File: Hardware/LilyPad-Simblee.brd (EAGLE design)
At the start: 45.3 x 45.2 mm, 37 parts, among them U1 MIC5219 3.3V, U2 MCP73831, U3 RFD77101

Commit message: Rep D8 w D6, add pour to antenna area, pour to top
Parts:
- moved C1 2.41 mm to (-17.3, -5.08)
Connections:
- removed net D8: A4/18.1, U3.20
- new net D6: A4/18.1, U3.31
- new net ISO_PAD: U3.1, U3.2, U3.4
- net GND: no longer U3.1, U3.2, U3.4
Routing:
- net D8: track 64.1 -> 0.00 mm, vias 1 -> 0
- net D6: track 0.00 -> 31.5 mm, vias 0 -> 1
- net ISO_PAD: track 0.00 -> 3.52 mm
- net GND: track 42.6 -> 41.0 mm, vias 15 -> 14
- net RST: track 52.7 -> 53.9 mm, vias 4 -> 5
- net 3.3V: track 39.8 -> 39.0 mm
- added copper zone on layer 1, net GND
- added copper zone on layer 1, net ISO_PAD

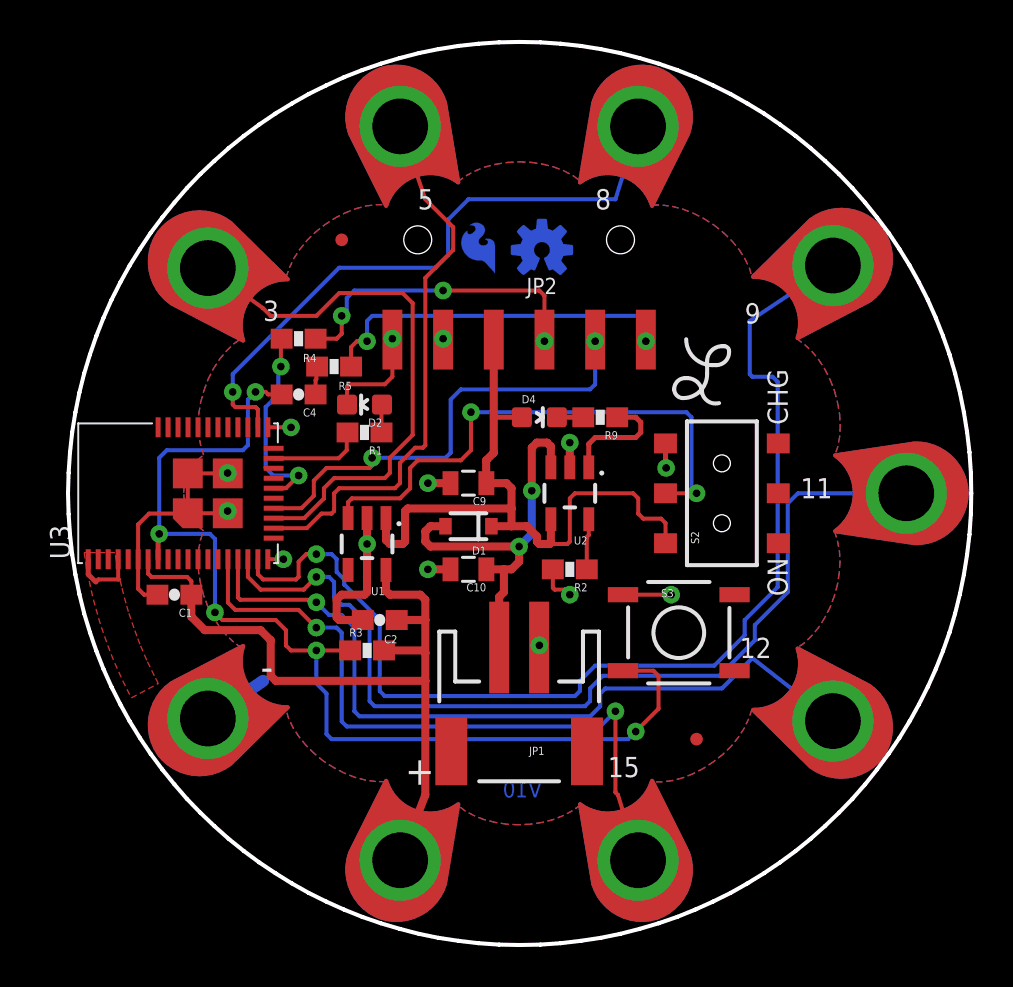
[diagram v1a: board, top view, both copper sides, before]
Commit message: Fix some QC review issues
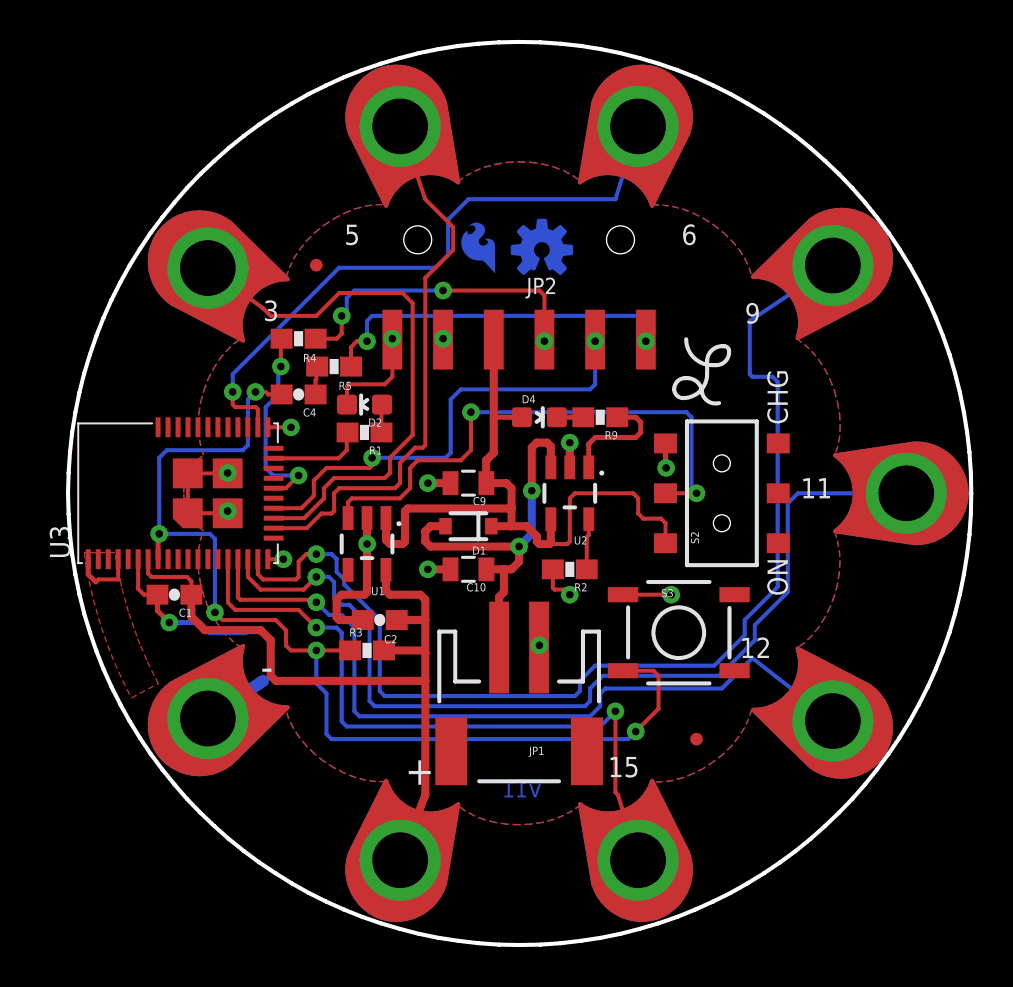
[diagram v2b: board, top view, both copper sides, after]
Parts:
- moved FID1 1.80 mm to (-10.2, 11.4)
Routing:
- net GND: track 41.0 -> 42.4 mm, vias 14 -> 15
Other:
- board text added: "6"
- board text added: "V11"
- board text removed: "8"
- board text removed: "V10"
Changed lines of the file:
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@@
 <wire x1="22.6364" y1="1.026125" x2="22.6564" y2="-0.003875" width="0.2032" layer="20"/>
 <text x="-12.827" y="8.636" size="1.016" layer="21" font="vector" ratio="15">3</text>
-<text x="-5.08" y="14.224" size="1.016" layer="21" font="vector" ratio="15">5</text>
-<text x="3.81" y="14.224" size="1.016" layer="21" font="vector" ratio="15">8</text>
+<text x="-8.763" y="12.446" size="1.016" layer="21" font="vector" ratio="15">5</text>
+<text x="8.128" y="12.446" size="1.016" layer="21" font="vector" ratio="15">6</text>
 <text x="11.303" y="8.509" size="1.016" layer="21" font="vector" ratio="15">9</text>
 <text x="14.097" y="-0.254" size="1.016" layer="21" font="vector" ratio="15">11</text>
@@
 <text x="-5.715" y="-14.605" size="1.4224" layer="21" font="vector" ratio="15">+</text>
 <text x="-12.954" y="-9.398" size="1.4224" layer="21" font="vector" ratio="15">-</text>
-<text x="1.143" y="-15.24" size="0.8128" layer="16" font="vector" ratio="15" rot="MR0">V10</text>
+<text x="1.143" y="-15.24" size="0.8128" layer="16" font="vector" ratio="15" rot="MR0">V11</text>
 <text x="22.86" y="-24.13" size="1.778" layer="51" font="vector" ratio="15">NOTE: Use 0.032" board thickness!</text>
 <text x="73.66" y="-31.75" size="1.778" layer="51" font="vector" ratio="15">Mike Hord</text>
@@
 <element name="LOGO1" library="SparkFun-Aesthetics" package="SFE_LOGO_FLAME_COPPER_.1" value="SFE_LOGO_FLAME.1COP" x="-0.889" y="10.668" rot="MR0"/>
 <element name="LOGO2" library="SparkFun-Aesthetics" package="OSHW-LOGO-S_COPPER" value="OSHW-LOGOS-COPPER" x="1.143" y="12.192" rot="MR0"/>
-<element name="FID1" library="SparkFun-Aesthetics" package="MICRO-FIDUCIAL" value="FIDUCIALUFIDUCIAL" x="-8.89" y="12.7"/>
+<element name="FID1" library="SparkFun-Aesthetics" package="MICRO-FIDUCIAL" value="FIDUCIALUFIDUCIAL" x="-10.16" y="11.43"/>
 <element name="FID2" library="SparkFun-Aesthetics" package="MICRO-FIDUCIAL" value="FIDUCIALUFIDUCIAL" x="8.89" y="-12.319"/>
 <element name="U$1" library="LilyPad-Wearables" package="LOGO-L" value="LOGO-LPL" x="9.144" y="6.096"/>
@@
 <wire x1="-18.796" y1="-5.08" x2="-19.09" y2="-4.786" width="0.2032" layer="1"/>
 <wire x1="-19.09" y1="-3.302" x2="-19.09" y2="-4.786" width="0.2032" layer="1"/>
-<wire x1="-19.09" y1="-3.302" x2="-19.09" y2="-1.564" width="0.2032" layer="1"/>
-<wire x1="-19.09" y1="-1.564" x2="-18.542" y2="-1.016" width="0.2032" layer="1"/>
-<wire x1="-18.542" y1="-1.016" x2="-16.614" y2="-1.016" width="0.2032" layer="1"/>
-<wire x1="-16.614" y1="-1.016" x2="-16.6" y2="-1.002" width="0.2032" layer="1"/>
 <polygon width="0.203" layer="1" isolate="0.3048" orphans="yes">
 <vertex x="-14.31" y="-7.45"/>
@@
 <vertex x="-13.92" y="-7.74"/>
 </polygon>
+<wire x1="-18.122" y1="-5.08" x2="-18.122" y2="-5.881" width="0.254" layer="1"/>
+<wire x1="-18.122" y1="-5.881" x2="-17.526" y2="-6.477" width="0.254" layer="1"/>
+<via x="-17.526" y="-6.477" extent="1-16" drill="0.381"/>
+<wire x1="-17.526" y1="-6.477" x2="-16.002" y2="-6.477" width="0.254" layer="16"/>
+<wire x1="-16.002" y1="-6.477" x2="-15.494" y2="-6.985" width="0.254" layer="16"/>
+<wire x1="-15.494" y1="-6.985" x2="-13.716" y2="-6.985" width="0.254" layer="16"/>
+<wire x1="-13.716" y1="-6.985" x2="-13.589" y2="-6.858" width="0.254" layer="16"/>
 </signal>
 <signal name="RST">

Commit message: Chg to V12, reduce paste on GND pads to 12.5%
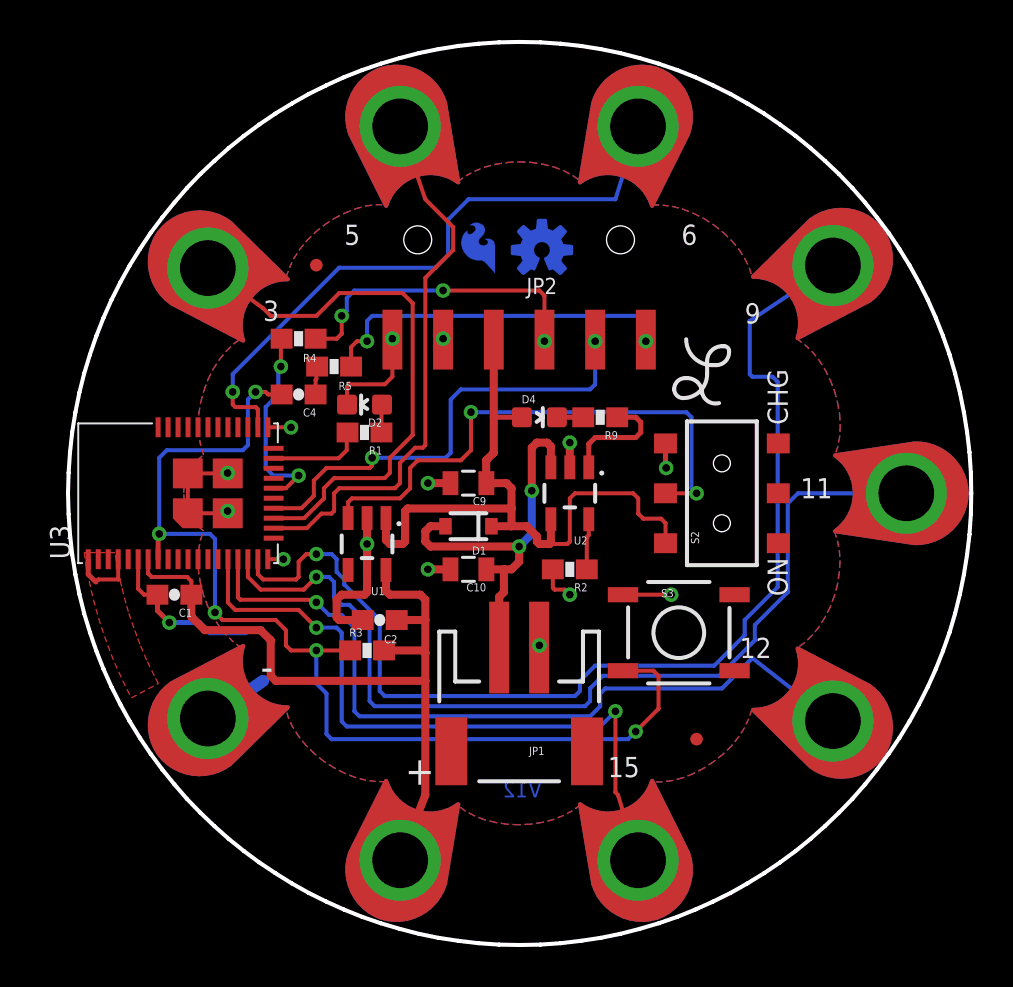
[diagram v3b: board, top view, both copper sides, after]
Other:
- board text added: "V12"
- board text removed: "V11"
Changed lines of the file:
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@@
 <layers>
 <layer number="1" name="Top" color="4" fill="1" visible="yes" active="yes"/>
-<layer number="2" name="Route2" color="1" fill="3" visible="yes" active="yes"/>
-<layer number="15" name="Route15" color="4" fill="6" visible="yes" active="yes"/>
+<layer number="2" name="Route2" color="1" fill="3" visible="no" active="yes"/>
+<layer number="15" name="Route15" color="4" fill="6" visible="no" active="yes"/>
 <layer number="16" name="Bottom" color="1" fill="1" visible="yes" active="yes"/>
 <layer number="17" name="Pads" color="2" fill="1" visible="yes" active="yes"/>
@@
 <layer number="23" name="tOrigins" color="15" fill="1" visible="yes" active="yes"/>
 <layer number="24" name="bOrigins" color="15" fill="1" visible="yes" active="yes"/>
-<layer number="25" name="tNames" color="7" fill="1" visible="yes" active="yes"/>
-<layer number="26" name="bNames" color="7" fill="1" visible="yes" active="yes"/>
-<layer number="27" name="tValues" color="7" fill="1" visible="yes" active="yes"/>
-<layer number="28" name="bValues" color="7" fill="1" visible="yes" active="yes"/>
-<layer number="29" name="tStop" color="5" fill="1" visible="yes" active="yes"/>
-<layer number="30" name="bStop" color="7" fill="6" visible="yes" active="yes"/>
-<layer number="31" name="tCream" color="7" fill="4" visible="yes" active="yes"/>
-<layer number="32" name="bCream" color="7" fill="5" visible="yes" active="yes"/>
-<layer number="39" name="tKeepout" color="4" fill="11" visible="yes" active="yes"/>
-<layer number="40" name="bKeepout" color="1" fill="11" visible="yes" active="yes"/>
-<layer number="41" name="tRestrict" color="4" fill="10" visible="yes" active="yes"/>
-<layer number="42" name="bRestrict" color="1" fill="10" visible="yes" active="yes"/>
-<layer number="43" name="vRestrict" color="2" fill="10" visible="yes" active="yes"/>
-<layer number="44" name="Drills" color="7" fill="1" visible="yes" active="yes"/>
+<layer number="25" name="tNames" color="7" fill="1" visible="no" active="yes"/>
+<layer number="26" name="bNames" color="7" fill="1" visible="no" active="yes"/>
+<layer number="27" name="tValues" color="7" fill="1" visible="no" active="yes"/>
+<layer number="28" name="bValues" color="7" fill="1" visible="no" active="yes"/>
+<layer number="29" name="tStop" color="5" fill="1" visible="no" active="yes"/>
+<layer number="30" name="bStop" color="7" fill="6" visible="no" active="yes"/>
+<layer number="31" name="tCream" color="7" fill="4" visible="no" active="yes"/>
+<layer number="32" name="bCream" color="7" fill="5" visible="no" active="yes"/>
+<layer number="39" name="tKeepout" color="4" fill="11" visible="no" active="yes"/>
+<layer number="40" name="bKeepout" color="1" fill="11" visible="no" active="yes"/>
+<layer number="41" name="tRestrict" color="4" fill="10" visible="no" active="yes"/>
+<layer number="42" name="bRestrict" color="1" fill="10" visible="no" active="yes"/>
+<layer number="43" name="vRestrict" color="2" fill="10" visible="no" active="yes"/>
+<layer number="44" name="Drills" color="7" fill="1" visible="no" active="yes"/>
 <layer number="45" name="Holes" color="7" fill="1" visible="yes" active="yes"/>
-<layer number="46" name="Milling" color="3" fill="1" visible="yes" active="yes"/>
-<layer number="47" name="Measures" color="7" fill="1" visible="yes" active="yes"/>
+<layer number="46" name="Milling" color="3" fill="1" visible="no" active="yes"/>
+<layer number="47" name="Measures" color="7" fill="1" visible="no" active="yes"/>
 <layer number="51" name="tDocu" color="6" fill="1" visible="yes" active="yes"/>
 <layer number="3" name="Route3" color="4" fill="3" visible="no" active="no"/>
@@
 <text x="-5.715" y="-14.605" size="1.4224" layer="21" font="vector" ratio="15">+</text>
 <text x="-12.954" y="-9.398" size="1.4224" layer="21" font="vector" ratio="15">-</text>
-<text x="1.143" y="-15.24" size="0.8128" layer="16" font="vector" ratio="15" rot="MR0">V11</text>
+<text x="1.143" y="-15.24" size="0.8128" layer="16" font="vector" ratio="15" rot="MR0">V12</text>
 <text x="22.86" y="-24.13" size="1.778" layer="51" font="vector" ratio="15">NOTE: Use 0.032" board thickness!</text>
 <text x="73.66" y="-31.75" size="1.778" layer="51" font="vector" ratio="15">Mike Hord</text>
@@
 </class>
 </classes>
-<designrules name="SparkFun-2-layer *">
-<description language="en">&lt;b&gt;EAGLE Design Rules&lt;/b&gt;
+<designrules name="SparkFun-2-layer-TIGHT">
+<description language="en">&lt;b&gt;SparkFun 2 Layer Design Rule Checks - STANDARD/TIGHT/FAB-LIMIT&lt;/b&gt;
 &lt;p&gt;
-The default Design Rules have been set to cover
-a wide range of applications. Your particular design
-may have different requirements, so please make the
-necessary adjustments and save your customized
-design rules under a new name.</description>
+These rules have been curated by SparkFuns DFM commitee. After doing much research, communicating with our multiple fab houses, and getting quotes of various designs, we have compiled three DRU files.
+&lt;p&gt;
+&lt;b&gt;STANDARD:&lt;/b&gt; This is more of a &quot;best case scenario&quot; set of limitations. If your design has the space, and/or you have the time to work within these parameters, please do. Larger trace width and clearance makes for easier visual inspection of the PCB while troubleshooting (useful in production and to the end user). It also allows for better ability to hack a trace (if you are crazy enough to scrape away the mask and solder to a trace). Another thing to keep in mind is that more metal is just more robust.
+&lt;p&gt;
+&lt;b&gt;TIGHT:&lt;/b&gt; This is where cost comes into play. We have found that most fab houses begin to add extra charges when you go smaller than these specs. In some cases, going to less than 15 mil trace can increase the cost by 10%. (This is why we have set the min drill on this DRU to 15 mil) Same story for traces thinner than 7 mil. To avoid those extra charges, then stay within the rules of this DRU.
+&lt;p&gt;
+&lt;b&gt;FAB-LIMIT:&lt;/b&gt; These set of rules are at the very limit of most fab houses capabilities. You will pay more for these specs, and it should be used on designs that have a darned good reason to need 4 mil vias and 4 mil traces.
+&lt;p&gt;
+**NOTE Clearance, Distance, Sizes, and Restring are all set to different limits in each of these three DRU files. Please compare the files within the CAM job editor window of eagle to see all the numbers.
+&lt;p&gt;
+***NOTE, Please set your Net Classes to default (0mil for all settings), so that it won't effect the DRC when you run it with these settings.</description>
 <param name="layerSetup" value="(1*16)"/>
 <param name="mtCopper" value="0.035mm 0.035mm 0.035mm 0.035mm 0.035mm 0.035mm 0.035mm 0.035mm 0.035mm 0.035mm 0.035mm 0.035mm 0.035mm 0.035mm 0.035mm 0.035mm"/>
 <param name="mtIsolate" value="1.5mm 0.15mm 0.2mm 0.15mm 0.2mm 0.15mm 0.2mm 0.15mm 0.2mm 0.15mm 0.2mm 0.15mm 0.2mm 0.15mm 0.2mm"/>
-<param name="mdWireWire" value="8mil"/>
-<param name="mdWirePad" value="8mil"/>
-<param name="mdWireVia" value="8mil"/>
-<param name="mdPadPad" value="8mil"/>
-<param name="mdPadVia" value="8mil"/>
-<param name="mdViaVia" value="8mil"/>
-<param name="mdSmdPad" value="8mil"/>
-<param name="mdSmdVia" value="8mil"/>
-<param name="mdSmdSmd" value="8mil"/>
+<param name="mdWireWire" value="7mil"/>
+<param name="mdWirePad" value="7mil"/>
+<param name="mdWireVia" value="7mil"/>
+<param name="mdPadPad" value="7mil"/>
+<param name="mdPadVia" value="7mil"/>
+<param name="mdViaVia" value="7mil"/>
+<param name="mdSmdPad" value="7mil"/>
+<param name="mdSmdVia" value="7mil"/>
+<param name="mdSmdSmd" value="7mil"/>
 <param name="mdViaViaSameLayer" value="8mil"/>
 <param name="mnLayersViaInSmd" value="2"/>
-<param name="mdCopperDimension" value="8mil"/>
-<param name="mdDrill" value="8mil"/>
+<param name="mdCopperDimension" value="7mil"/>
+<param name="mdDrill" value="7mil"/>
 <param name="mdSmdStop" value="0mil"/>
 <param name="msWidth" value="7mil"/>
-<param name="msDrill" value="12mil"/>
+<param name="msDrill" value="15mil"/>
 <param name="msMicroVia" value="9.99mm"/>
 <param name="msBlindViaRatio" value="0.5"/>
@@
 <param name="rvMicroViaOuter" value="0.25"/>
 <param name="rvMicroViaInner" value="0.25"/>
-<param name="rlMinPadTop" value="12mil"/>
+<param name="rlMinPadTop" value="7mil"/>
 <param name="rlMaxPadTop" value="20mil"/>
-<param name="rlMinPadInner" value="10mil"/>
+<param name="rlMinPadInner" value="7mil"/>
 <param name="rlMaxPadInner" value="20mil"/>
-<param name="rlMinPadBottom" value="12mil"/>
+<param name="rlMinPadBottom" value="7mil"/>
 <param name="rlMaxPadBottom" value="20mil"/>
-<param name="rlMinViaOuter" value="10mil"/>
+<param name="rlMinViaOuter" value="7mil"/>
 <param name="rlMaxViaOuter" value="20mil"/>
-<param name="rlMinViaInner" value="10mil"/>
+<param name="rlMinViaInner" value="7mil"/>
 <param name="rlMaxViaInner" value="20mil"/>
 <param name="rlMinMicroViaOuter" value="4mil"/>
